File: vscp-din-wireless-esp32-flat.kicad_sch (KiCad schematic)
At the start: 19 parts, among them J1 Screw_Terminal_01x15, J3 Conn_01x06, U1 ESP32-WROOM-32E, U2 R-78B3.3-2.0

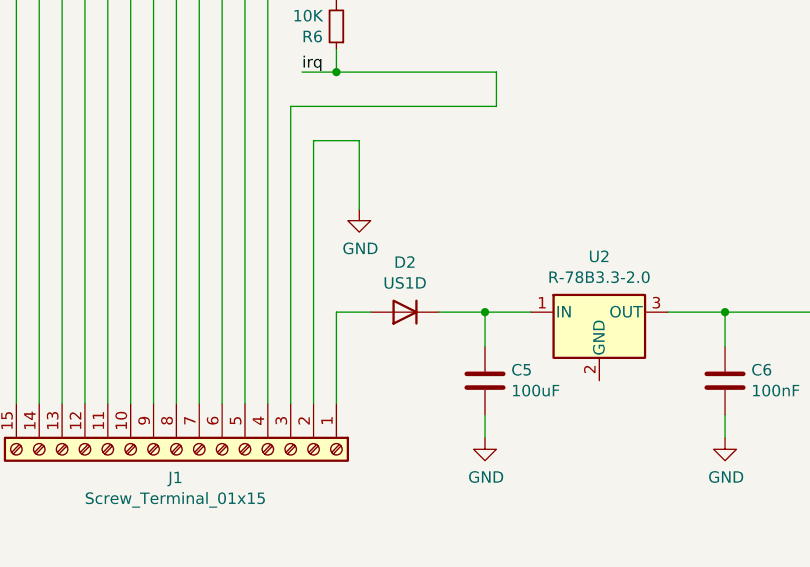
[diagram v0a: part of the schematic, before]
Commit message: Changed power input diod to SS34
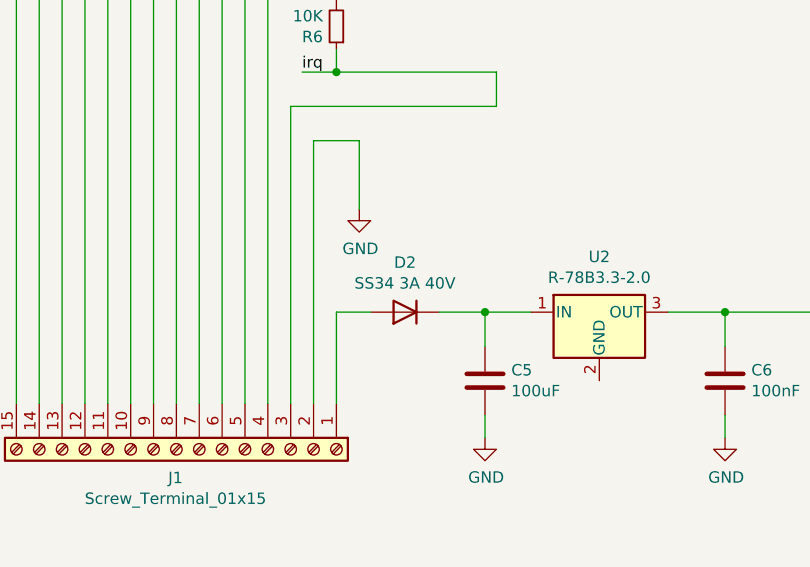
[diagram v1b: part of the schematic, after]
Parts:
- D2: value US1D -> SS34 3A 40V
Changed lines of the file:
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@@
 			)
 		)
-		(property "Value" "US1D"
+		(property "Value" "SS34 3A 40V"
 			(at 119.38 161.8996 0)
 			(effects
